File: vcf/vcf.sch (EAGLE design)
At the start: 104 parts, among them IC1 OPA4130U, IC2 OPA4130U, IC3 OPA4130U, IC4 OPA4130U, IC5 OPA4130U, Q1 BC847ASMD, Q2 BC847ASMD, Q3 BC847ASMD, Q4 BC847ASMD, Q5 BC847ASMD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

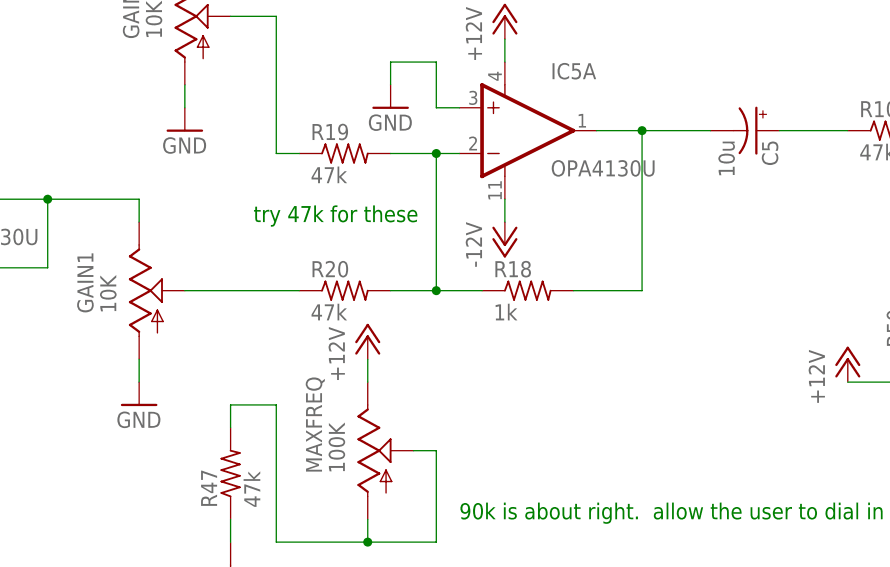
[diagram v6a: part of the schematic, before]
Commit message: added notes in schem about reducing input attenuation resistors
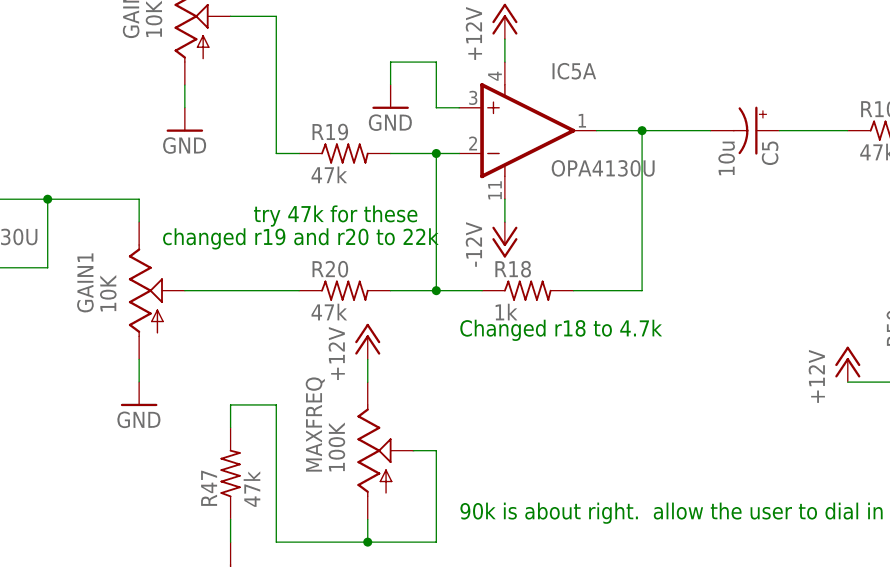
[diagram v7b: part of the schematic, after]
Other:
- note added: "Changed r18 to 4.7k"
- note added: "changed r19 and r20 to 22k"
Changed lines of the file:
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@@
 <text x="119.38" y="88.9" size="1.778" layer="91">22k is about right</text>
 <text x="-53.34" y="-5.08" size="1.778" layer="91">90k is about right.  allow the user to dial in a good feel for the knob</text>
+<text x="-53.34" y="15.24" size="1.778" layer="91">Changed r18 to 4.7k</text>
+<text x="-86.36" y="25.4" size="1.778" layer="91">changed r19 and r20 to 22k</text>
 </plain>
 <instances>
